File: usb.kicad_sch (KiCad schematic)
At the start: 90 parts, among them J16 USB-C_GCT_USB4105-GF-A, J4 USB-C_GCT_USB4105-GF-A

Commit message: [#54617] Update FT4233 symbol from lib
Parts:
- U?: footprint antmicro-footprints:QFN-76-1EP_9x9mm_P0.4mm_EP3.8x3.8mm -> antmicro-footprints:QFN-76-1EP_9x9mm_P0.4mm_EP6.3x6.3mm
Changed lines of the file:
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@@
       (effects (font (size 1.27 1.27) (thickness 0.15)) (justify left bottom) hide)
     )
-    (property "Footprint" "antmicro-footprints:QFN-76-1EP_9x9mm_P0.4mm_EP3.8x3.8mm" (at 382.27 146.05 0)
+    (property "Footprint" "antmicro-footprints:QFN-76-1EP_9x9mm_P0.4mm_EP6.3x6.3mm" (at 382.27 146.05 0)
       (effects (font (size 1.27 1.27) (thickness 0.15)) (justify left bottom) hide)
     )

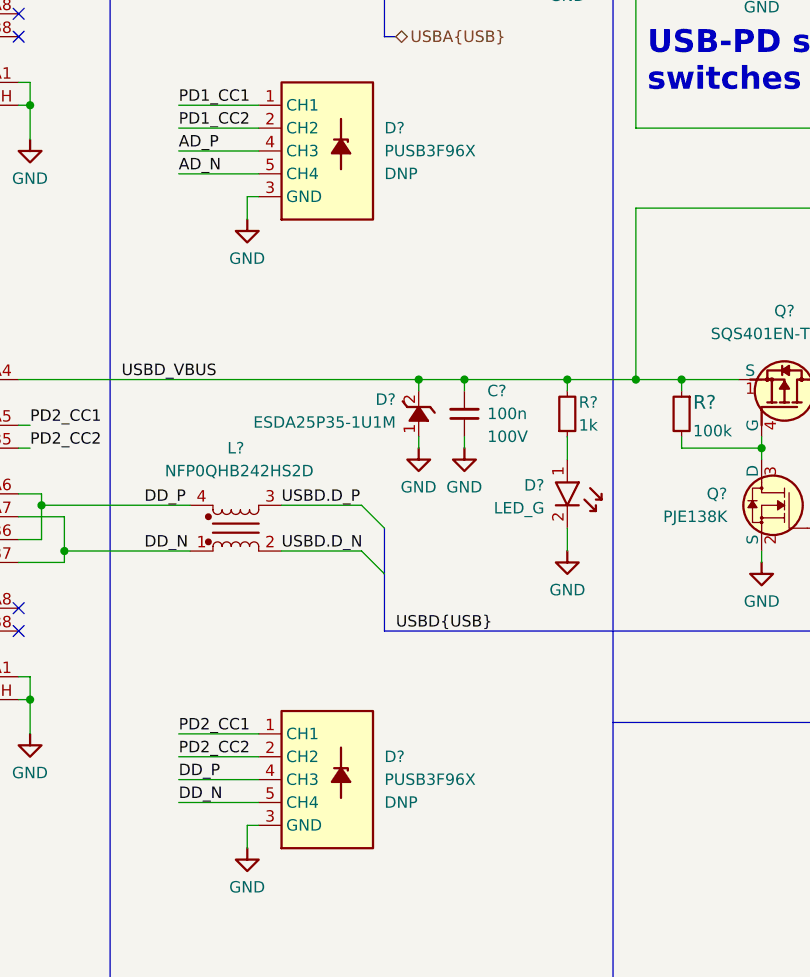
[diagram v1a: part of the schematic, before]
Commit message: [#54617] Update bus naming; remove DNP for TVS
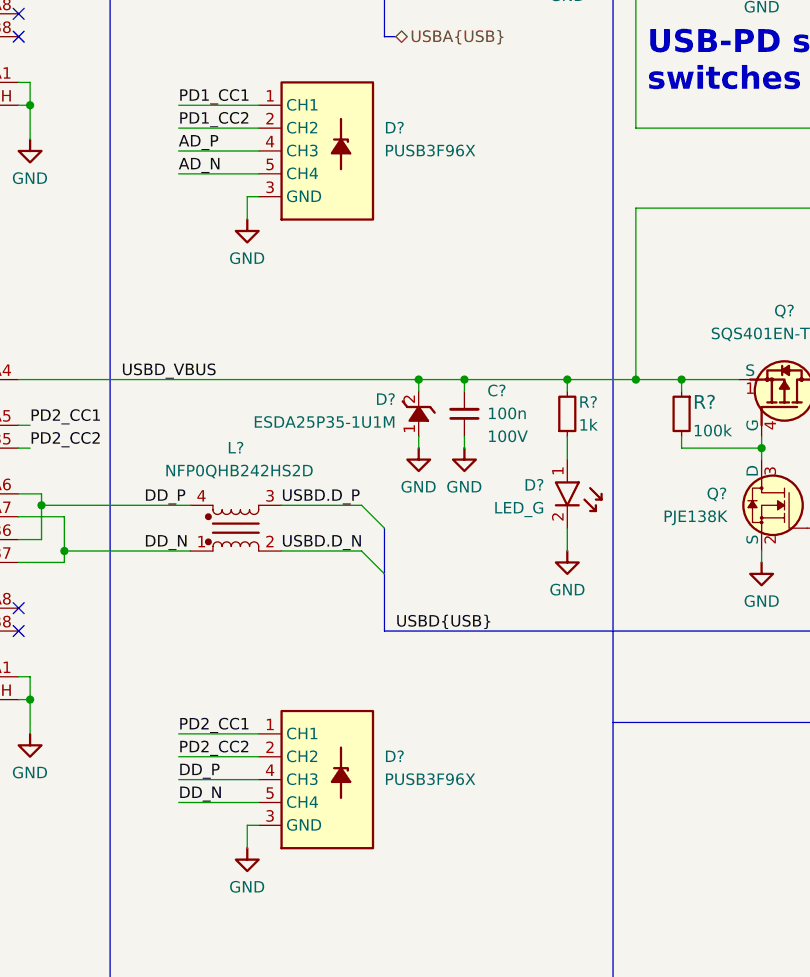
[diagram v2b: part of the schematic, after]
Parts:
- D? (x2): DNP DNP -> (none)
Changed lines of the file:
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@@
       (effects (font (size 1.27 1.27) (thickness 0.15)) (justify left bottom) hide)
-    )
-    (property "DNP" "DNP" (at 78.74 110.4899 0)
-      (effects (font (size 1.27 1.27)) (justify left))
     )
     (pin "1")
@@
       (effects (font (size 1.27 1.27) (thickness 0.15)) (justify left bottom) hide)
     )
-    (property "DNP" "DNP" (at 78.74 180.3399 0)
-      (effects (font (size 1.27 1.27)) (justify left))
-    )
     (pin "1")

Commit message: [#54617] Review requested changes
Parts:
- C? (x2): MPN MC0402N180J500CT -> CL05C180JB51PNC; Manufacturer Multicomp -> Samsung Electro-Mechanics
- Q? (x4): Manufacturer Panjit -> PANJIT
- U?: MPN AP22615AWU-7 -> AP22615AWU-7
- U?: Manufacturer Microchip -> Microchip Technology

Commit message: [#54617] Re-enumerate reference designators
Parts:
- gave numbers to parts that had none: 88
- renumbered J4 to J901, J16 to J902

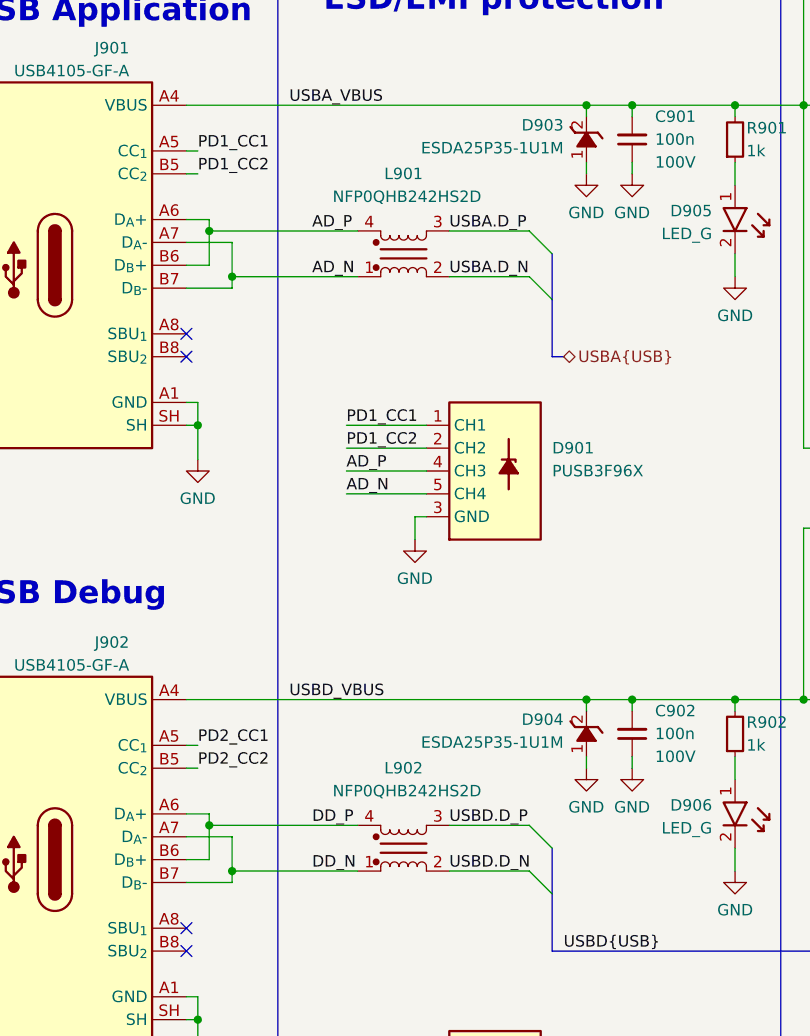
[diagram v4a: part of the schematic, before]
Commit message: [#54617] Remove CM chokes for HDMI & DSI; change CM chokes for USB
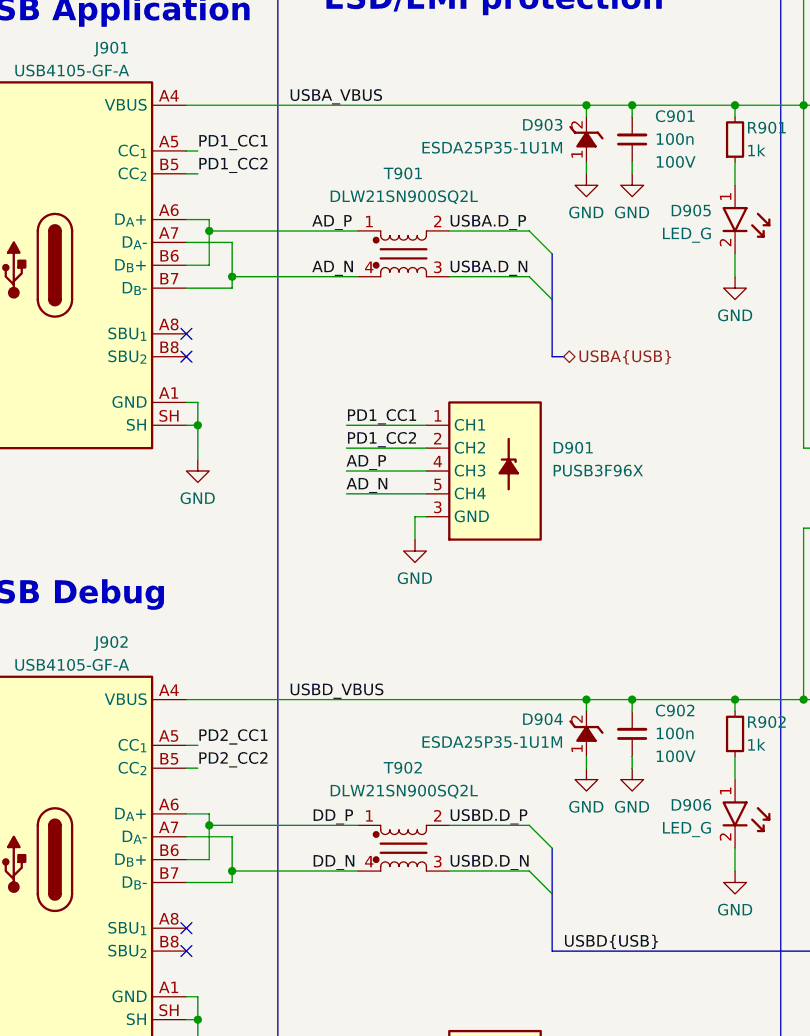
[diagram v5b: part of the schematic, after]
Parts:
- removed L901, L902: NFP0QHB242HS2D, antmicro-footprints:Choke_025020_0605Metric, symbol antmicroCommonModeChokes:Choke_NFP0QHB242HS2D
- added T901, T902: Choke_DLW21SN900SQ2L, antmicro-footprints:Choke_Murata-DLW21, symbol antmicroCommonModeChokes:Choke_DLW21SN900SQ2L
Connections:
- net AD_N: now also T901.4
- net AD_P: now also T901.1
- net DD_N: now also T902.4
- net DD_P: now also T902.1
- net USBA.D_N: now also T901.3
- net USBA.D_P: now also T901.2
- net USBD.D_N: now also T902.3
- net USBD.D_P: now also T902.2
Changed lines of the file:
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@@
     )
   )
+  (symbol (lib_id "antmicroCommonModeChokes:Choke_DLW21SN900SQ2L") (at 57.15 81.28 0) (unit 1)
+    (in_bom yes) (on_board yes) (dnp no)
+    (property "Reference" "T901" (at 62.23 74.93 0)
+      (effects (font (size 1.27 1.27) (thickness 0.15)))
+    )
+    (property "Value" "Choke_DLW21SN900SQ2L" (at 72.39 91.44 0)
+      (effects (font (size 1.27 1.27) (thickness 0.15)) (justify left bottom) hide)
+    )
+    (property "Footprint" "antmicro-footprints:Choke_Murata-DLW21" (at 72.39 93.98 0)
+      (effects (font (size 1.27 1.27) (thickness 0.15)) (justify left bottom) hide)
+    )
+    (property "Datasheet" "https://www.murata.com/en-us/products/productdetail?partno=DLW21SN900SQ2%23" (at 72.39 96.52 0)
+      (effects (font (size 1.27 1.27) (thickness 0.15)) (justify left bottom) hide)
+    )
+    (property "Manufacturer" "Murata" (at 72.39 99.06 0)
+      (effects (font (size 1.27 1.27) (thickness 0.15)) (justify left bottom) hide)
+    )
+    (property "MPN" "DLW21SN900SQ2L" (at 62.23 77.47 0)
+      (effects (font (size 1.27 1.27) (thickness 0.15)))
+    )
+    (property "IMax" "0.33 A" (at 72.39 101.6 0)
+      (effects (font (size 1.27 1.27) (thickness 0.15)) (justify left bottom) hide)
+    )
+    (property "Author" "Antmicro" (at 72.39 104.14 0)
+      (effects (font (size 1.27 1.27) (thickness 0.15)) (justify left bottom) hide)
+    )
+    (property "License" "Apache-2.0" (at 72.39 106.68 0)
+      (effects (font (size 1.27 1.27) (thickness 0.15)) (justify left bottom) hide)
+    )
+    (pin "4")
+    (pin "1")
+    (pin "2")
+    (pin "3")
+    (instances
+      (project "cm4-baseboard"
+        (path "/60b842dc-0853-4a25-99ac-5784ddf94d0d/6e132e8a-be93-4f6c-b030-15293fb6e15c"
+          (reference "T901") (unit 1)
+        )
+      )
+    )
+  )
   (symbol (lib_id "antmicroResistors0402:R_1k_0402") (at 99.06 73.66 90) (unit 1)
     (in_bom yes) (on_board yes) (dnp no)
@@
     )
   )
-  (symbol (lib_id "antmicroCommonModeChokes:Choke_NFP0QHB242HS2D") (at 57.15 86.36 0) (mirror x) (unit 1)
-    (in_bom yes) (on_board yes) (dnp no)
-    (property "Reference" "L901" (at 62.23 74.93 0)
-      (effects (font (size 1.27 1.27) (thickness 0.15)))
-    )
-    (property "Value" "NFP0QHB242HS2D" (at 88.9 78.74 0)
-      (effects (font (size 1.27 1.27) (thickness 0.15)) (justify left bottom) hide)
-    )
-    (property "Footprint" "antmicro-footprints:Choke_025020_0605Metric" (at 72.39 73.66 0)
-      (effects (font (size 1.27 1.27) (thickness 0.15)) (justify left bottom) hide)
-    )
-    (property "Datasheet" "https://www.murata.com/products/productdetail?partno=NFP0QHB242HS2%23" (at 72.39 71.12 0)
-      (effects (font (size 1.27 1.27) (thickness 0.15)) (justify left bottom) hide)
-    )
-    (property "MPN" "NFP0QHB242HS2D" (at 62.611 77.47 0)
-      (effects (font (size 1.27 1.27) (thickness 0.15)))
-    )
-    (property "Manufacturer" "Murata" (at 72.39 68.58 0)
-      (effects (font (size 1.27 1.27) (thickness 0.15)) (justify left bottom) hide)
-    )
-    (property "Author" "Antmicro" (at 72.39 63.5 0)
-      (effects (font (size 1.27 1.27) (thickness 0.15)) (justify left bottom) hide)
-    )
-    (property "License" "Apache-2.0" (at 72.39 60.96 0)
-      (effects (font (size 1.27 1.27) (thickness 0.15)) (justify left bottom) hide)
-    )
-    (property "IMax" "0.1 A" (at 72.39 66.04 0)
-      (effects (font (size 1.27 1.27) (thickness 0.15)) (justify left bottom) hide)
-    )
-    (pin "1")
-    (pin "2")
-    (pin "3")
-    (pin "4")
-    (instances
-      (project "cm4-baseboard"
-        (path "/60b842dc-0853-4a25-99ac-5784ddf94d0d/6e132e8a-be93-4f6c-b030-15293fb6e15c"
-          (reference "L901") (unit 1)
-        )
-      )
-    )
-  )
   (symbol (lib_id "antmicropower:GND") (at 250.19 151.13 0) (unit 1)
     (in_bom yes) (on_board yes) (dnp no) (fields_autoplaced)
@@
     )
   )
+  (symbol (lib_id "antmicroCommonModeChokes:Choke_DLW21SN900SQ2L") (at 57.15 147.32 0) (unit 1)
+    (in_bom yes) (on_board yes) (dnp no)
+    (property "Reference" "T902" (at 62.23 140.97 0)
+      (effects (font (size 1.27 1.27) (thickness 0.15)))
+    )
+    (property "Value" "Choke_DLW21SN900SQ2L" (at 72.39 157.48 0)
+      (effects (font (size 1.27 1.27) (thickness 0.15)) (justify left bottom) hide)
+    )
+    (property "Footprint" "antmicro-footprints:Choke_Murata-DLW21" (at 72.39 160.02 0)
+      (effects (font (size 1.27 1.27) (thickness 0.15)) (justify left bottom) hide)
+    )
+    (property "Datasheet" "https://www.murata.com/en-us/products/productdetail?partno=DLW21SN900SQ2%23" (at 72.39 162.56 0)
+      (effects (font (size 1.27 1.27) (thickness 0.15)) (justify left bottom) hide)
+    )
+    (property "Manufacturer" "Murata" (at 72.39 165.1 0)
+      (effects (font (size 1.27 1.27) (thickness 0.15)) (justify left bottom) hide)
+    )
+    (property "MPN" "DLW21SN900SQ2L" (at 62.23 143.51 0)
+      (effects (font (size 1.27 1.27) (thickness 0.15)))
+    )
+    (property "IMax" "0.33 A" (at 72.39 167.64 0)
+      (effects (font (size 1.27 1.27) (thickness 0.15)) (justify left bottom) hide)
+    )
+    (property "Author" "Antmicro" (at 72.39 170.18 0)
+      (effects (font (size 1.27 1.27) (thickness 0.15)) (justify left bottom) hide)
+    )
+    (property "License" "Apache-2.0" (at 72.39 172.72 0)
+      (effects (font (size 1.27 1.27) (thickness 0.15)) (justify left bottom) hide)
+    )
+    (pin "4")
+    (pin "1")
+    (pin "2")
+    (pin "3")
+    (instances
+      (project "cm4-baseboard"
+        (path "/60b842dc-0853-4a25-99ac-5784ddf94d0d/6e132e8a-be93-4f6c-b030-15293fb6e15c"
+          (reference "T902") (unit 1)
+        )
+      )
+    )
+  )
   (symbol (lib_id "antmicroTVSDiodes:PUSB3F96X_PASS") (at 64.77 102.87 0) (unit 1)
     (in_bom yes) (on_board yes) (dnp no) (fields_autoplaced)
@@
         )
       )
-    )
-  )
-  (symbol (lib_id "antmicroCommonModeChokes:Choke_NFP0QHB242HS2D") (at 57.15 152.4 0) (mirror x) (unit 1)
-    (in_bom yes) (on_board yes) (dnp no)
-    (property "Reference" "L902" (at 62.23 140.97 0)
-      (effects (font (size 1.27 1.27) (thickness 0.15)))
-    )
-    (property "Value" "NFP0QHB242HS2D" (at 88.9 144.78 0)
-      (effects (font (size 1.27 1.27) (thickness 0.15)) (justify left bottom) hide)
-    )
-    (property "Footprint" "antmicro-footprints:Choke_025020_0605Metric" (at 72.39 139.7 0)
-      (effects (font (size 1.27 1.27) (thickness 0.15)) (justify left bottom) hide)
-    )
-    (property "Datasheet" "https://www.murata.com/products/productdetail?partno=NFP0QHB242HS2%23" (at 72.39 137.16 0)
-      (effects (font (size 1.27 1.27) (thickness 0.15)) (justify left bottom) hide)
-    )
-    (property "MPN" "NFP0QHB242HS2D" (at 62.611 143.51 0)
-      (effects (font (size 1.27 1.27) (thickness 0.15)))
-    )
-    (property "Manufacturer" "Murata" (at 72.39 134.62 0)
-      (effects (font (size 1.27 1.27) (thickness 0.15)) (justify left bottom) hide)
-    )
-    (property "Author" "Antmicro" (at 72.39 129.54 0)
-      (effects (font (size 1.27 1.27) (thickness 0.15)) (justify left bottom) hide)
-    )
-    (property "License" "Apache-2.0" (at 72.39 127 0)
-      (effects (font (size 1.27 1.27) (thickness 0.15)) (justify left bottom) hide)
-    )
-    (property "IMax" "0.1 A" (at 72.39 132.08 0)
-      (effects (font (size 1.27 1.27) (thickness 0.15)) (justify left bottom) hide)
-    )
-    (pin "1")
-    (pin "2")
-    (pin "3")
-    (pin "4")
-    (instances
-      (project "cm4-baseboard"
-        (path "/60b842dc-0853-4a25-99ac-5784ddf94d0d/6e132e8a-be93-4f6c-b030-15293fb6e15c"
-          (reference "L902") (unit 1)
-        )
-      )

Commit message: [#55247] Change USB schematic: Remove PD from App USB, add CC controller
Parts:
- removed C901: C_100n_100V_0805, antmicro-footprints:C_0805_2012Metric, symbol antmicroCapacitorsmisc:C_100n_100V_0805
- removed C908: C_100n_0402, antmicro-footprints:C_0402_1005Metric, symbol antmicroCapacitors0402:C_100n_0402
- removed D903: ESDA25P35-1U1M, antmicro-footprints:ESDA25P35-1U1M, symbol antmicroTVSDiodes:ESDA25P35-1U1M
- removed D908: RB521S30T1G, antmicro-footprints:SOD-523, symbol antmicroDiodesRectifiersSingle:RB521S30T1G
- removed Q901: SQS401EN-T1_BE3, antmicro-footprints:Vishay_PowerPAK_1212-8_Single, symbol antmicroTransistorsFETsMOSFETsSingle:SQS401EN-T1_BE3
- removed Q903: PJE138K, antmicro-footprints:SOT-523, symbol antmicroTransistorsFETsMOSFETsSingle:PJE138K
- removed R903: R_100k_0402, antmicro-footprints:R_0402_1005Metric, symbol antmicroResistors0402:R_100k_0402
- removed R905: R_2k2_0402, antmicro-footprints:R_0402_1005Metric, symbol antmicroResistors0402:R_2k2_0402
- removed R915: R_15k_0402, antmicro-footprints:R_0402_1005Metric, symbol antmicroResistors0402:R_15k_0402
- added C901, C928, C930: C_100n_0402, antmicro-footprints:C_0402_1005Metric, symbol antmicroCapacitors0402:C_100n_0402
- added C908: C_10u_0402, antmicro-footprints:C_0402_1005Metric, symbol antmicroCapacitors0402:C_10u_0402
- added C929: C_Pol_330u_6.3V_KEMET-T520-B, antmicro-footprints:C_Pol_EIA-B, symbol antmicroCapacitorspol:C_Pol_330u_6.3V_KEMET-T520-B
- added C931: C_1u_25V_0402, antmicro-footprints:C_0402_1005Metric, symbol antmicroCapacitors0402:C_1u_25V_0402
- added D903: PESD5Z5_0F, antmicro-footprints:SOD-523, symbol antmicroTVSDiodes:PESD5Z5_0F
- added Q901: PJE138K, antmicro-footprints:SOT-523, symbol antmicroTransistorsFETsMOSFETsSingle:PJE138K
- added Q903: SSM3J332R, antmicro-footprints:SOT-23-3, symbol antmicroTransistorsFETsMOSFETsSingle:SSM3J332R
- added R903: R_910k_0402, antmicro-footprints:R_0402_1005Metric, symbol antmicroResistors0402:R_910k_0402
- added R905, R927, R928: R_4k7_0402, antmicro-footprints:R_0402_1005Metric, symbol antmicroResistors0402:R_4k7_0402
- added R915: R_470k_0402, antmicro-footprints:R_0402_1005Metric, symbol antmicroResistors0402:R_470k_0402
- added R924, R925: R_100k_0402, antmicro-footprints:R_0402_1005Metric, symbol antmicroResistors0402:R_100k_0402
- added R926: R_100R_0402, antmicro-footprints:R_0402_1005Metric, symbol antmicroResistors0402:R_100R_0402
- added TP909, TP910, TP911, TP912, TP913, TP914, TP915, TP916, TP917: TP_0.75mm_SMD, antmicro-footprints:TP_SMD_0.75mm, symbol antmicroTestPoints:TP_0.75mm_SMD
- added U906: TUSB321RWBR, antmicro-footprints:Texas_X2QFN-12_1.6x1.6mm_P0.4mm, symbol antmicroInterfaceControllers:TUSB321RWBR
- U902: value 93LC66BT_DFN -> 93AA66C; footprint antmicro-footprints:DFN-8-1EP_3x2mm_P0.5mm_EP1.36x1.46mm -> antmicro-footprints:SOIC-8_3.9x4.9x1.75mm_P1.27mm; symbol antmicroMemory:93LC66BT_DFN -> antmicroMemory:93AA66C_SOIC; MPN 93LC66BT-I/MC -> 93AA66C-I/SN
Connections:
- net USBD_VBUS is gone; now on net V_{BUS}: C902.2, D904.2 (A), D909.2, J902.A4 (VBUS), J902.A9 (VBUS), J902.B4 (VBUS), J902.B9 (VBUS), Q902.1 (S), Q902.2 (S), Q902.3 (S), R902.2, R904.1, R916.1, R918.1
- net +5V: now also C931.2, Q903.2 (S), R926.1, R928.2; no longer C904.1, U901.6 (IN)
- net GND: now also C901.2, C908.1, C928.2, C929.2, D903.2, Q901.2 (S), R905.1, R925.2, R927.1, U906.10 (GND); no longer U902.9 (EP)
- net USBA_VBUS: now also C901.1, C908.2, D903.1, R903.1; no longer R914.1
- net at U901.5 (ISET): now also R905.2
- net PD1_CC1 renamed USBA_CC1
- net USBA_CC1: now also U906.1 (CC1); no longer U905.70 (PD1_CC1)
- net PD1_CC2 renamed USBA_CC2
- net USBA_CC2: now also U906.2 (CC2); no longer U905.67 (PD1_CC2)
- net PD1_EN renamed USBD_IN_EN
- net USBD_IN_EN: now also Q904.1 (G)
- net PD1_OUT_EN: no longer names the net of U905.7 (GPIO5)
- net PD1_OUT_EN: now also TP917.1; no longer U901.4 (EN)
- removed net PD1_SVBUS: R914.2, TP901.1, U905.68 (PD1_SVBUS)
- net PD2_CC1 renamed USBD_CC1
- net USBD_CC1: now also U905.70 (PD1_CC1); no longer U905.71 (PD2_CC1)
- net PD2_CC2 renamed USBD_CC2
- net USBD_CC2: now also U905.67 (PD1_CC2); no longer U905.73 (PD2_CC2)
- net PD2_EN: no longer names the net of U905.6 (GPIO4)
- net PD2_EN: now also TP916.1; no longer Q904.1 (G)
- net PD2_SVBUS renamed USBD_SVBUS
- net USBD_SVBUS: now also U905.68 (PD1_SVBUS); no longer U905.72 (PD2_SVBUS)
- new net: TP912.1, U906.8 (OUT2)
- new net: TP915.1, U905.73 (PD2_CC2)
- new net: TP913.1, U905.72 (PD2_SVBUS)
- new net: R915.1, U906.3 (CURRENT_MODE)
- new net: C930.1, C931.1, Q903.1 (G), R927.2, R928.1
- new net: TP910.1, U906.6 (~{VCONN_FAULT})
- new net: TP901.1, U906.11 (DIR)
- new net: R903.2, U906.5 (VBUS_DET)
- new net: TP911.1, U906.7 (OUT1)
- new net: TP914.1, U905.71 (PD2_CC1)
- new net: TP909.1, U906.4 (PORT)
- new net +3V3: R924.1
- new net +5V_{CAP}: C904.1, C928.1, C929.1, C930.2, Q903.3 (D), R914.1, R915.2, R925.1, R926.2, U901.6 (IN), U906.12 (VDD)
- new net USBA.OTGID: Q901.1 (G), R924.2, U906.9 (ID)
- new net USBA_OUT_EN: Q901.3 (D), R914.2, U901.4 (EN)
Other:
- note added: "FT4233 EEPROM"
- note added: "FT4233 power selector"
- note added: "ISET = 1.5A"
- note added: "USB CC controller"
- note added: "USB source Cap. with soft-start"
- note added: "USB source switch"
- note added: "USB-PD sink switch"
- note added: "Use main 5V supply (if available) Otherwise use power from debug USB port (5-15V) [USB power is used, only until main dcdc starts] [main 5V is preffered as results in higher LDO efficiency, in USB-PD scenario]"
- note removed: "EEPROM"
- note removed: "FD4233 power selector"
- note removed: "ISET = 3A"
- note removed: "USB-PD sink switches"
- note removed: "USB-PD source switch"
- note removed: "Use main 5V supply (if available) Otherwise use power from any USB port (5-20V) [USB power is used, only until main dcdc starts] [main 5V is preffered as results in higher LDO efficiency, in USB-PD scenario]"
- moved on the sheet: C902, C903, C904, C905, C906, C907, C909, C910, C911, C912, C913, C914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
